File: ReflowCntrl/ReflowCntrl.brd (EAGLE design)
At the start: 86 x 50.8 mm, 13 parts, among them J1 DCJ0202, T1 2N2222

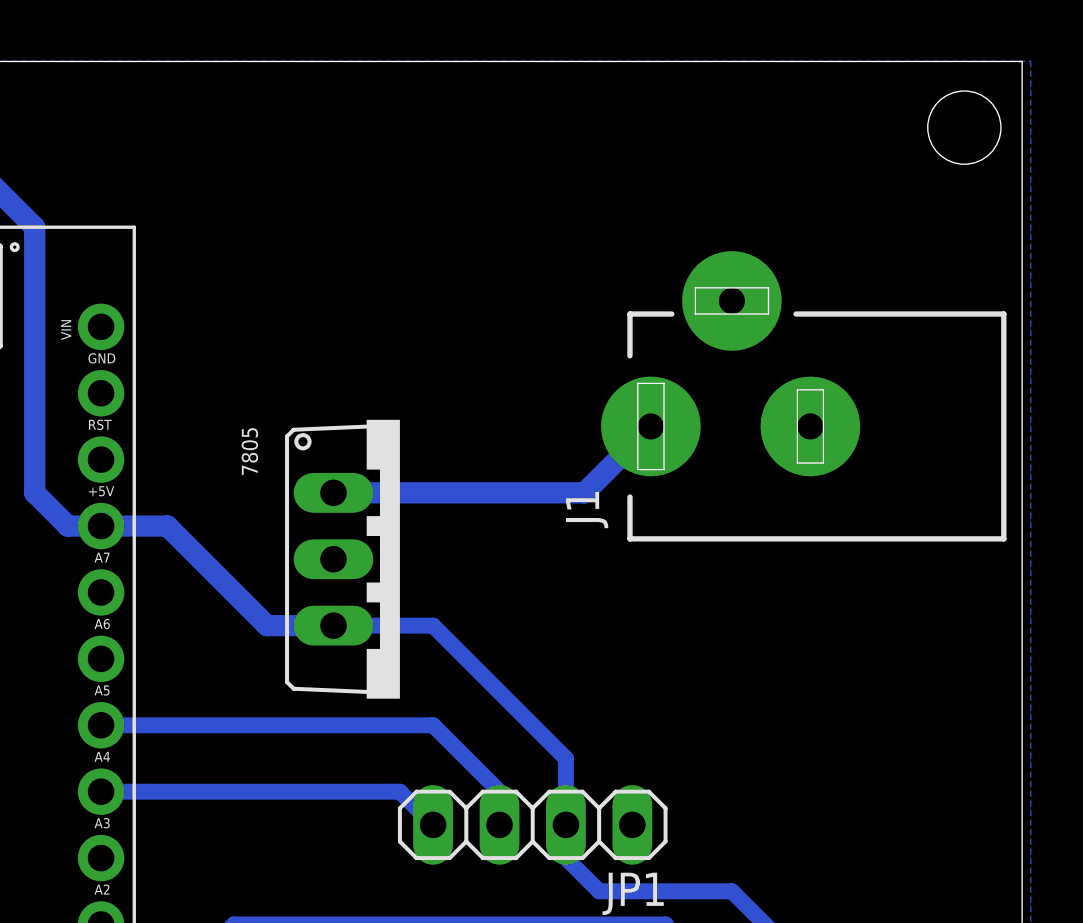
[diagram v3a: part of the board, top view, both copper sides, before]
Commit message: Move the DC jack so the 7805 can lay flat.
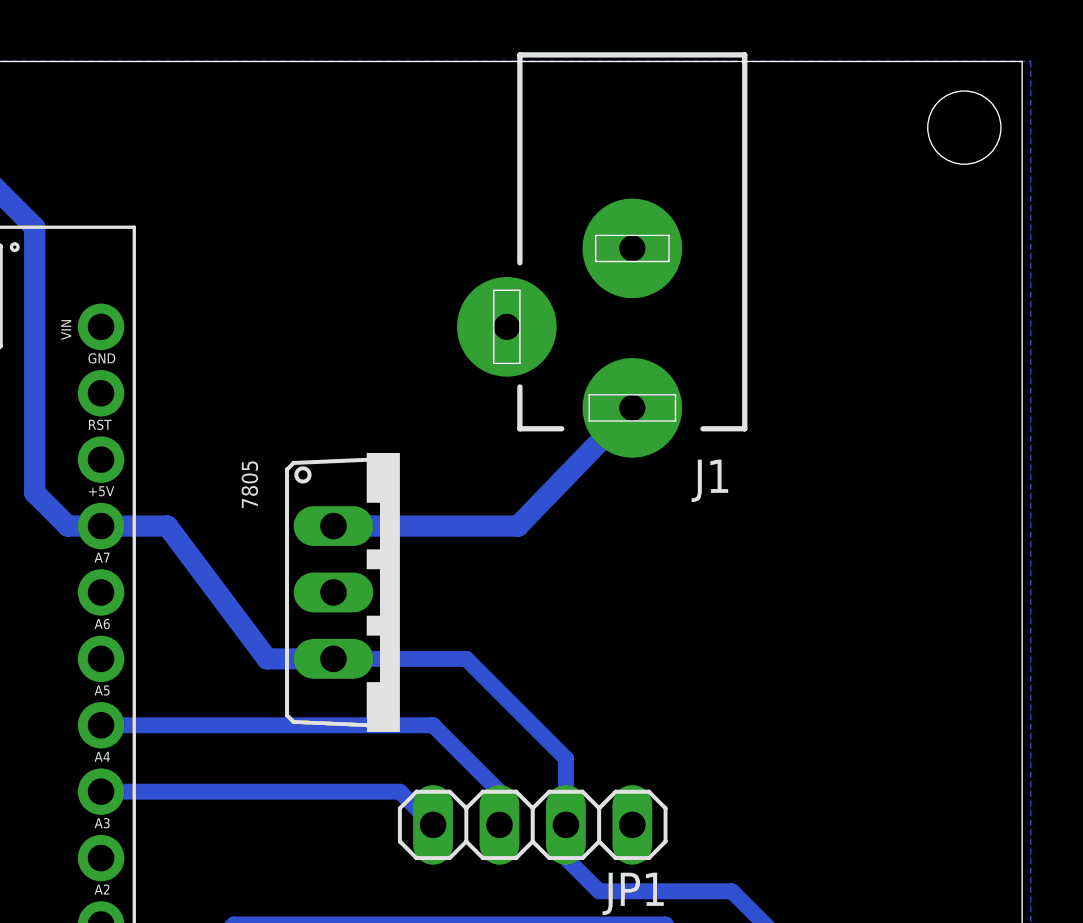
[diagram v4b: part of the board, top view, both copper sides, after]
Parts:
- moved J1 5.39 mm to (71.1, 40.6), turned to 180 degrees
- moved U$1 1.27 mm to (62.2, 30.5)
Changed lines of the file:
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@@
 </autorouter>
 <elements>
-<element name="J1" library="con-jack-jke" package="DCJ0202" value="DCJ0202" x="74.93" y="36.83" rot="R90">
-<attribute name="MPN" value="" x="74.93" y="36.83" size="1.778" layer="27" rot="R90" display="off"/>
-<attribute name="MF" value="" x="74.93" y="36.83" size="1.778" layer="27" rot="R90" display="off"/>
-<attribute name="OC_FARNELL" value="unknown" x="74.93" y="36.83" size="1.778" layer="27" rot="R90" display="off"/>
-<attribute name="OC_NEWARK" value="unknown" x="74.93" y="36.83" size="1.778" layer="27" rot="R90" display="off"/>
+<element name="J1" library="con-jack-jke" package="DCJ0202" value="DCJ0202" x="71.12" y="40.64" rot="R180">
+<attribute name="MPN" value="" x="71.12" y="40.64" size="1.778" layer="27" rot="R180" display="off"/>
+<attribute name="MF" value="" x="71.12" y="40.64" size="1.778" layer="27" rot="R180" display="off"/>
+<attribute name="OC_FARNELL" value="unknown" x="71.12" y="40.64" size="1.778" layer="27" rot="R180" display="off"/>
+<attribute name="OC_NEWARK" value="unknown" x="71.12" y="40.64" size="1.778" layer="27" rot="R180" display="off"/>
 </element>
 <element name="JP1" library="pinhead" package="1X04" value="OLED" x="67.31" y="21.59" rot="R180"/>
@@
 </element>
 <element name="T1" library="adafruit" package="TO92-EBC-OVAL" value="2N2222" x="27.94" y="22.86" rot="R270"/>
-<element name="U$1" library="LM7805" package="TO220AV" value="7805-TO220V" x="62.23" y="31.75" rot="R270"/>
+<element name="U$1" library="LM7805" package="TO220AV" value="7805-TO220V" x="62.23" y="30.48" rot="R270"/>
 <element name="X2" library="con-wago-508" package="W237-132" value="" x="12.7" y="8.89" rot="R270">
 <attribute name="OC_NEWARK" value="unknown" x="12.7" y="8.89" size="1.778" layer="27" rot="R270" display="off"/>
@@
 <wire x1="48.26" y1="44.45" x2="45.72" y2="46.99" width="0.8128" layer="16"/>
 <wire x1="50.8" y1="33.02" x2="53.34" y2="33.02" width="0.8128" layer="16"/>
-<wire x1="53.34" y1="33.02" x2="57.15" y2="29.21" width="0.8128" layer="16"/>
-<wire x1="57.15" y1="29.21" x2="59.69" y2="29.21" width="0.8128" layer="16"/>
+<wire x1="53.34" y1="33.02" x2="57.15" y2="27.94" width="0.8128" layer="16"/>
+<wire x1="57.15" y1="27.94" x2="59.69" y2="27.94" width="0.8128" layer="16"/>
 <wire x1="69.85" y1="2.54" x2="68.58" y2="3.81" width="0.6096" layer="16"/>
 <wire x1="68.58" y1="3.81" x2="68.58" y2="12.7" width="0.6096" layer="16"/>
@@
 <wire x1="72.39" y1="15.24" x2="68.58" y2="12.7" width="0.6096" layer="16"/>
 <contactref element="JP1" pad="2"/>
-<wire x1="59.69" y1="29.21" x2="63.5" y2="29.21" width="0.6096" layer="16"/>
-<wire x1="63.5" y1="29.21" x2="68.58" y2="24.13" width="0.6096" layer="16"/>
+<wire x1="59.69" y1="27.94" x2="64.77" y2="27.94" width="0.6096" layer="16"/>
+<wire x1="64.77" y1="27.94" x2="68.58" y2="24.13" width="0.6096" layer="16"/>
 <wire x1="68.58" y1="24.13" x2="68.58" y2="21.59" width="0.6096" layer="16"/>
 <wire x1="68.58" y1="21.59" x2="68.58" y2="20.32" width="0.6096" layer="16"/>
@@
 <contactref element="J1" pad="1"/>
 <contactref element="U$1" pad="VI"/>
-<wire x1="59.69" y1="34.29" x2="69.29" y2="34.29" width="0.8128" layer="16"/>
-<wire x1="69.29" y1="34.29" x2="71.83" y2="36.83" width="0.8128" layer="16"/>
+<wire x1="59.69" y1="33.02" x2="66.75" y2="33.02" width="0.8128" layer="16"/>
+<wire x1="66.75" y1="33.02" x2="71.12" y2="37.54" width="0.8128" layer="16"/>
 </signal>
 <signal name="SDA">
